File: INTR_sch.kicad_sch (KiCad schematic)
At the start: 10 parts, among them U18 8259A

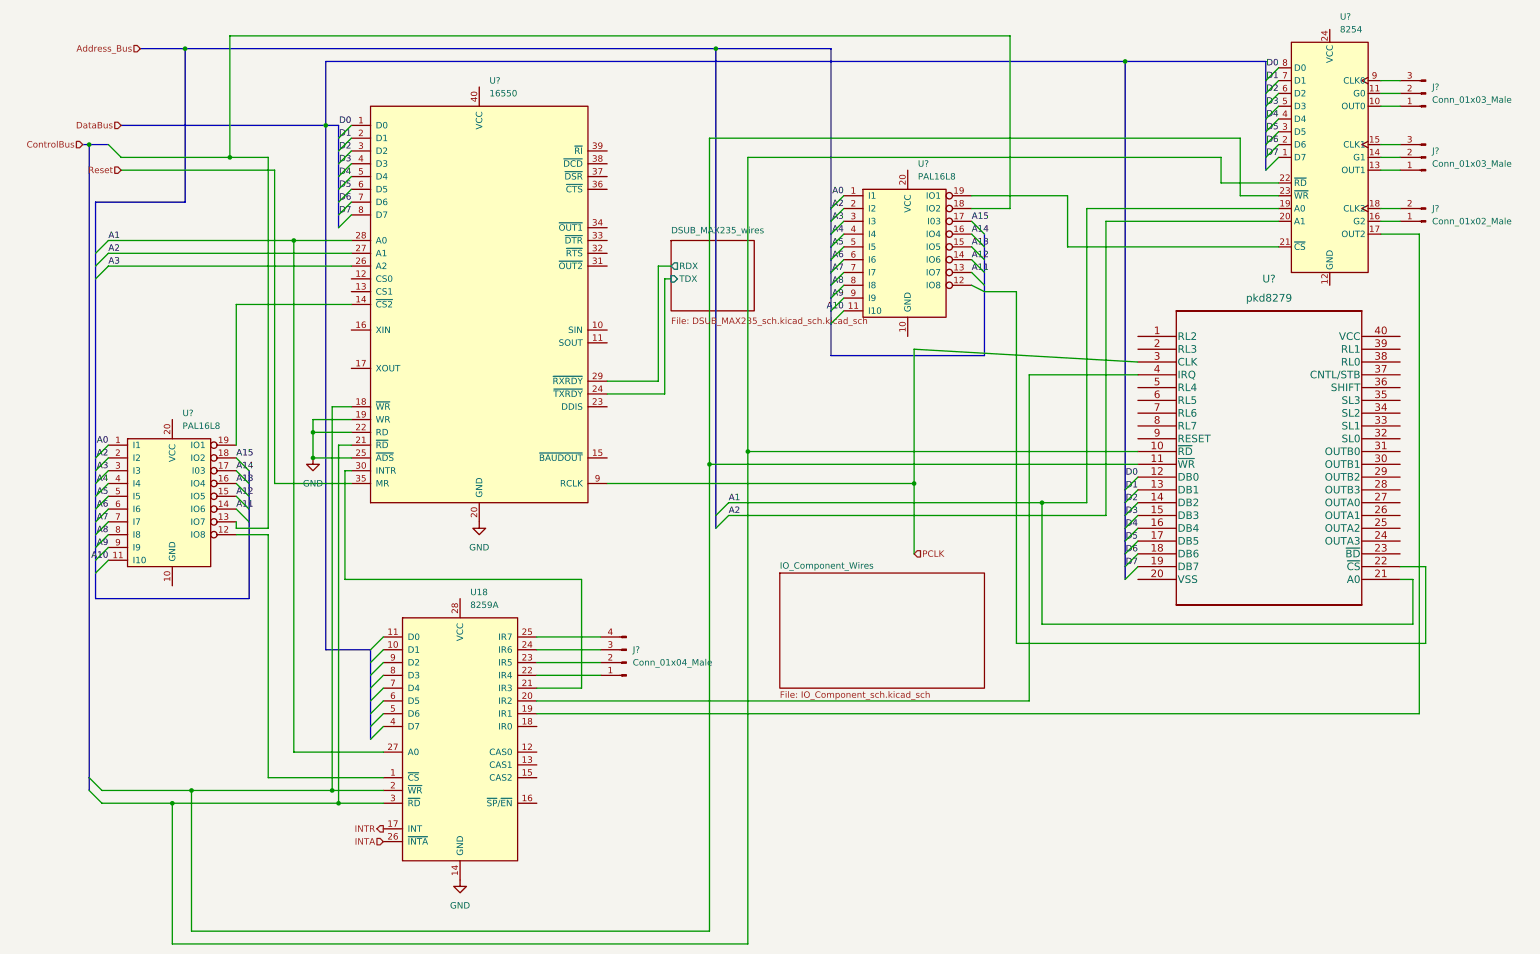
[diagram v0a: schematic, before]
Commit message: Fixed some wires
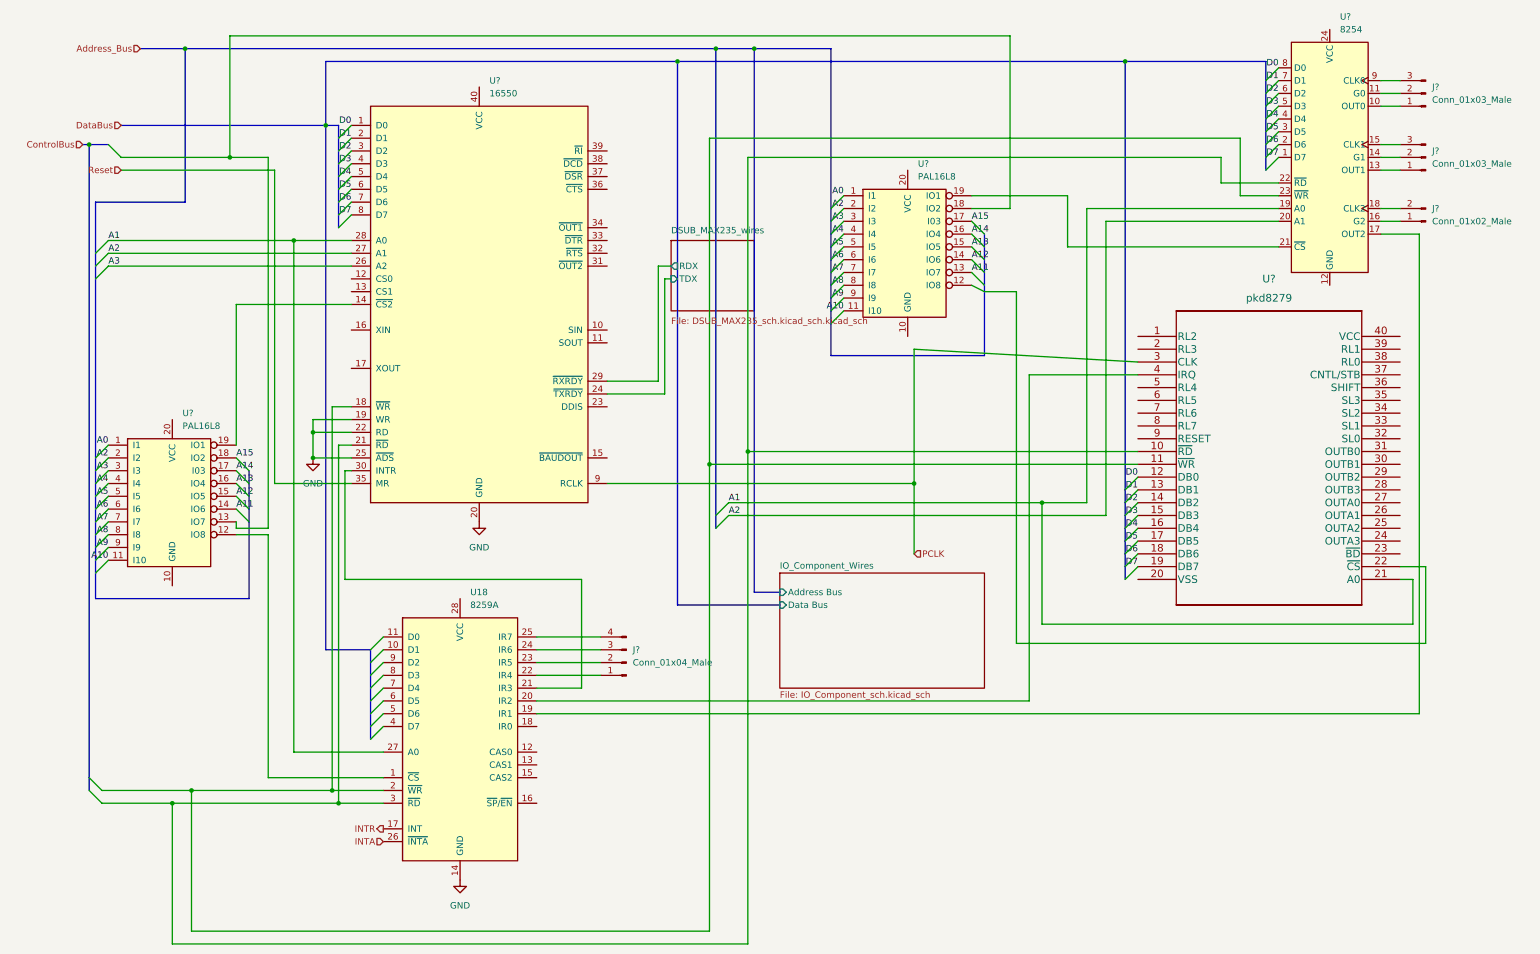
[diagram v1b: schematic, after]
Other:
- sheet IO_Component_Wires ports: added Address Bus, Data Bus; removed none
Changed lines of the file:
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@@
   (junction (at 62.23 93.98) (diameter 0) (color 0 0 0 0)
   )
+  (junction (at 149.86 17.78) (diameter 0) (color 0 0 0 0)
+  )
   (junction (at 66.04 165.1) (diameter 0) (color 0 0 0 0)
   )
+  (junction (at 134.62 20.32) (diameter 0) (color 0 0 0 0)
+  )
   (bus_entry (at 142.24 113.03) (size 2.54 -2.54)
     (stroke (width 0) (type default) (color 0 0 0 0))
@@
     (stroke (width 0) (type default) (color 0 0 0 0))
   )
+  (bus (pts (xy 134.62 128.27) (xy 154.94 128.27))
+    (stroke (width 0) (type default) (color 0 0 0 0))
+  )
   (wire (pts (xy 144.78 107.95) (xy 207.01 107.95))
     (stroke (width 0) (type default) (color 0 0 0 0))
@@
     (stroke (width 0) (type default) (color 0 0 0 0))
   )
+  (bus (pts (xy 134.62 20.32) (xy 134.62 128.27))
+    (stroke (width 0) (type default) (color 0 0 0 0))
+  )
   (bus (pts (xy 73.66 137.16) (xy 64.77 137.16))
     (stroke (width 0) (type default) (color 0 0 0 0))
@@
     (stroke (width 0) (type default) (color 0 0 0 0))
   )
-  (bus (pts (xy 142.24 17.78) (xy 165.1 17.78))
+  (bus (pts (xy 142.24 17.78) (xy 149.86 17.78))
     (stroke (width 0) (type default) (color 0 0 0 0))
   )
@@
     (stroke (width 0) (type default) (color 0 0 0 0))
   )
+  (bus (pts (xy 149.86 125.73) (xy 154.94 125.73))
+    (stroke (width 0) (type default) (color 0 0 0 0))
+  )
   (wire (pts (xy 34.29 167.64) (xy 34.29 195.58))
     (stroke (width 0) (type default) (color 0 0 0 0))
@@
     (stroke (width 0) (type default) (color 0 0 0 0))
   )
+  (bus (pts (xy 149.86 17.78) (xy 165.1 17.78))
+    (stroke (width 0) (type default) (color 0 0 0 0))
+  )
   (wire (pts (xy 45.72 39.37) (xy 53.34 39.37))
     (stroke (width 0) (type default) (color 0 0 0 0))
@@
     (stroke (width 0) (type default) (color 0 0 0 0))
   )
+  (bus (pts (xy 134.62 20.32) (xy 223.52 20.32))
+    (stroke (width 0) (type default) (color 0 0 0 0))
+  )
   (bus (pts (xy 19.05 99.06) (xy 19.05 63.5))
     (stroke (width 0) (type default) (color 0 0 0 0))
@@
     (stroke (width 0) (type default) (color 0 0 0 0))
   )
-  (bus (pts (xy 64.77 20.32) (xy 223.52 20.32))
+  (bus (pts (xy 64.77 20.32) (xy 134.62 20.32))
     (stroke (width 0) (type default) (color 0 0 0 0))
   )
@@
   )
   (bus (pts (xy 49.53 104.14) (xy 49.53 106.68))
+    (stroke (width 0) (type default) (color 0 0 0 0))
+  )
+  (bus (pts (xy 149.86 17.78) (xy 149.86 125.73))
     (stroke (width 0) (type default) (color 0 0 0 0))
   )
@@
       (effects (font (size 1.27 1.27)) (justify left top))
     )
-  )
+    (pin "Address Bus" input (at 154.94 125.73 180)
+      (effects (font (size 1.27 1.27)) (justify left))
+    )
+    (pin "Data Bus" input (at 154.94 128.27 180)
+      (effects (font (size 1.27 1.27)) (justify left))
+    )
+  )

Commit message: Finished wiring and decoding IO devices (except for push button switches)
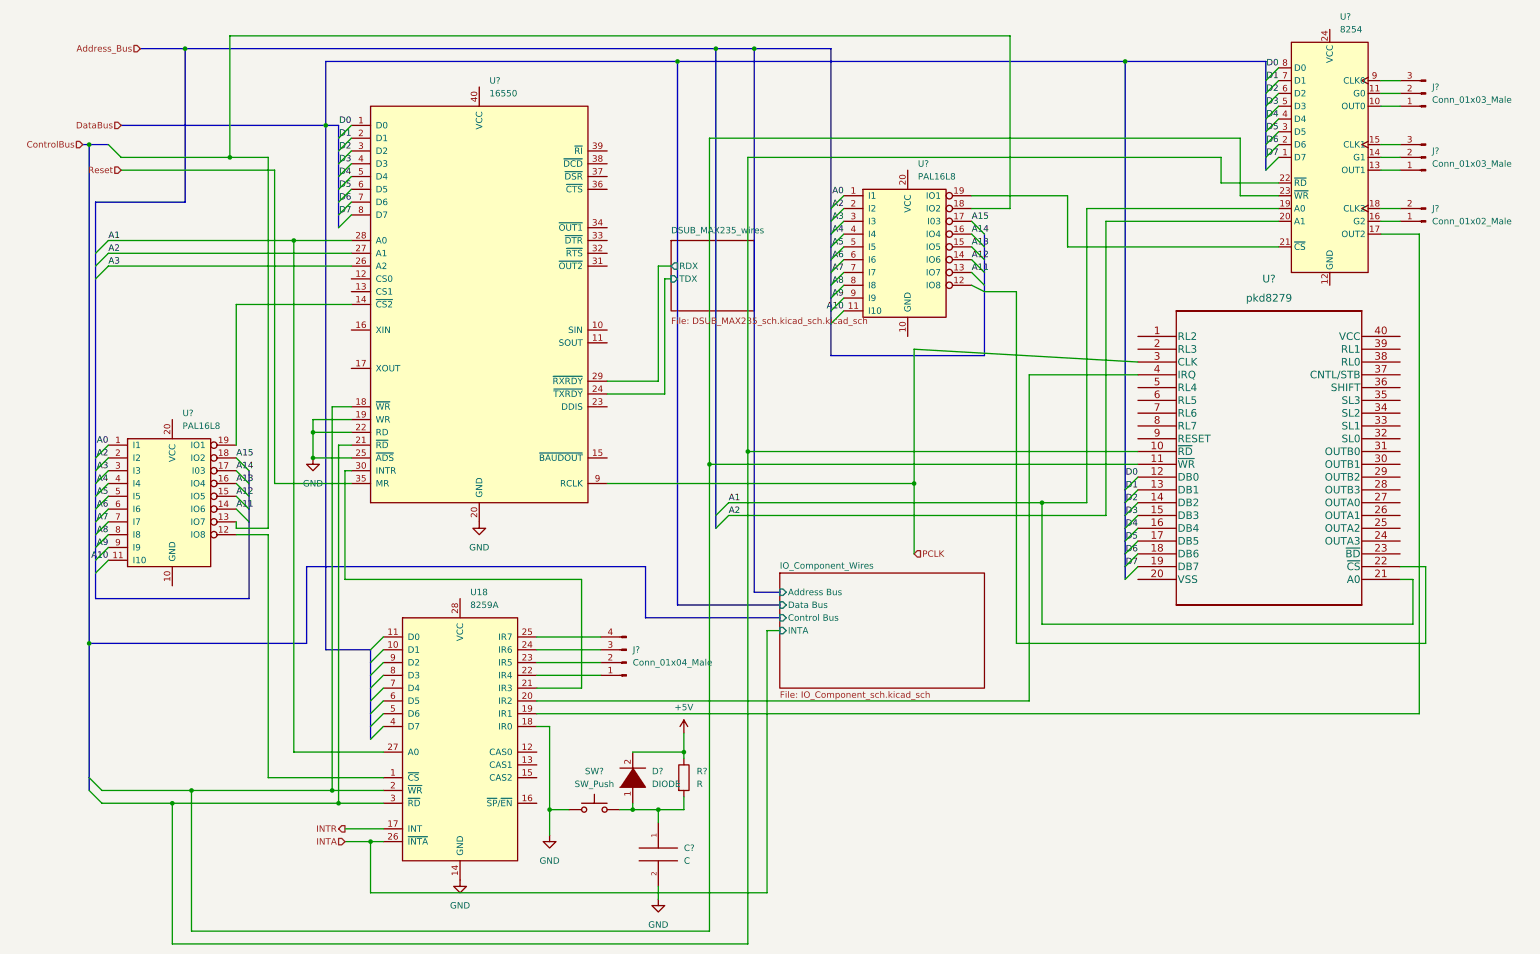
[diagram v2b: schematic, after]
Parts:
- added C?: C, symbol pspice:C
- added D?: DIODE, symbol pspice:DIODE
- added R?: R, symbol Device:R
- added SW?: SW_Push, symbol Switch:SW_Push
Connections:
- net GND: now also U18.18 (IR0), C?.2, SW?.1
- new net: C?.1, D?.1 (K), R?.2, SW?.2
- new net +5V: D?.2 (A), R?.1
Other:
- sheet IO_Component_Wires ports: added Control Bus, INTA; removed none

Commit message: Wired Push Buttons and added footprints
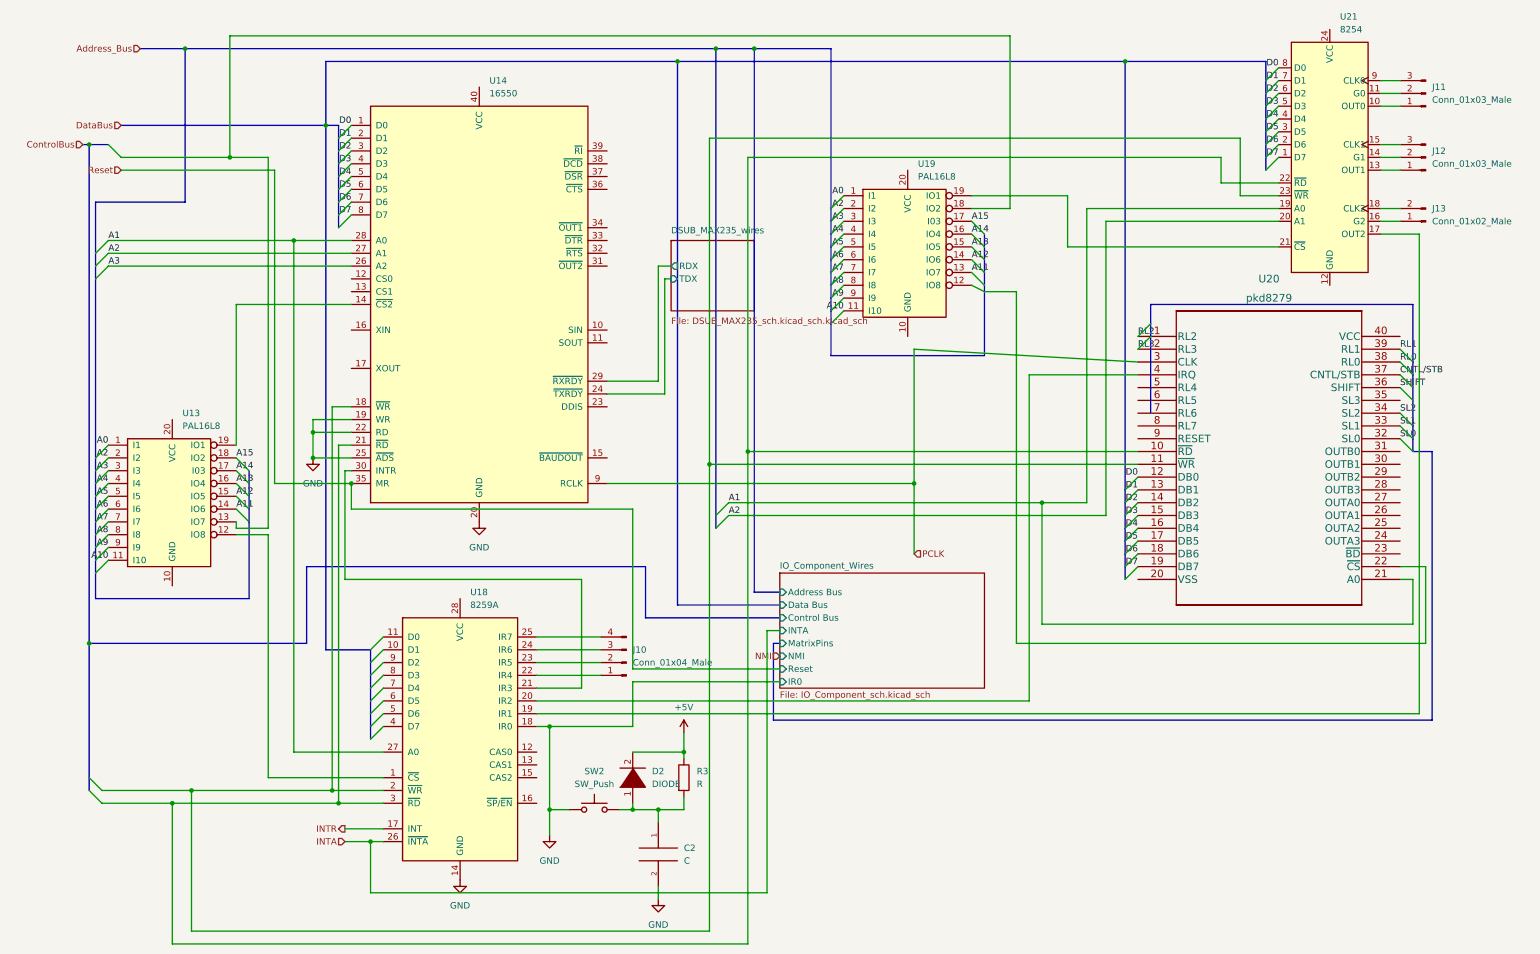
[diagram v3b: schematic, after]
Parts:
- U20: renamed from U?; footprint pkd8279 -> (none)
- gave numbers to parts that had none: 12
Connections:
- net RL2: now reaches U20.1 (RL2)
- net RL3: now reaches U20.2 (RL3)
- net SL0: now reaches U20.32 (SL0)
- net SL1: now reaches U20.33 (SL1)
- net SL2: now reaches U20.34 (SL2)
- net SHIFT: now reaches U20.36 (SHIFT)
- net CNTL/STB: now reaches U20.37 (CNTL/STB)
- net RL0: now reaches U20.38 (RL0)
- net RL1: now reaches U20.39 (RL1)
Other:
- sheet IO_Component_Wires ports: added IR0, MatrixPins, NMI, Reset; removed none

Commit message: Added power and ground to chips
Added power and ground to chips as well as checked and added all labels for pins off of busses
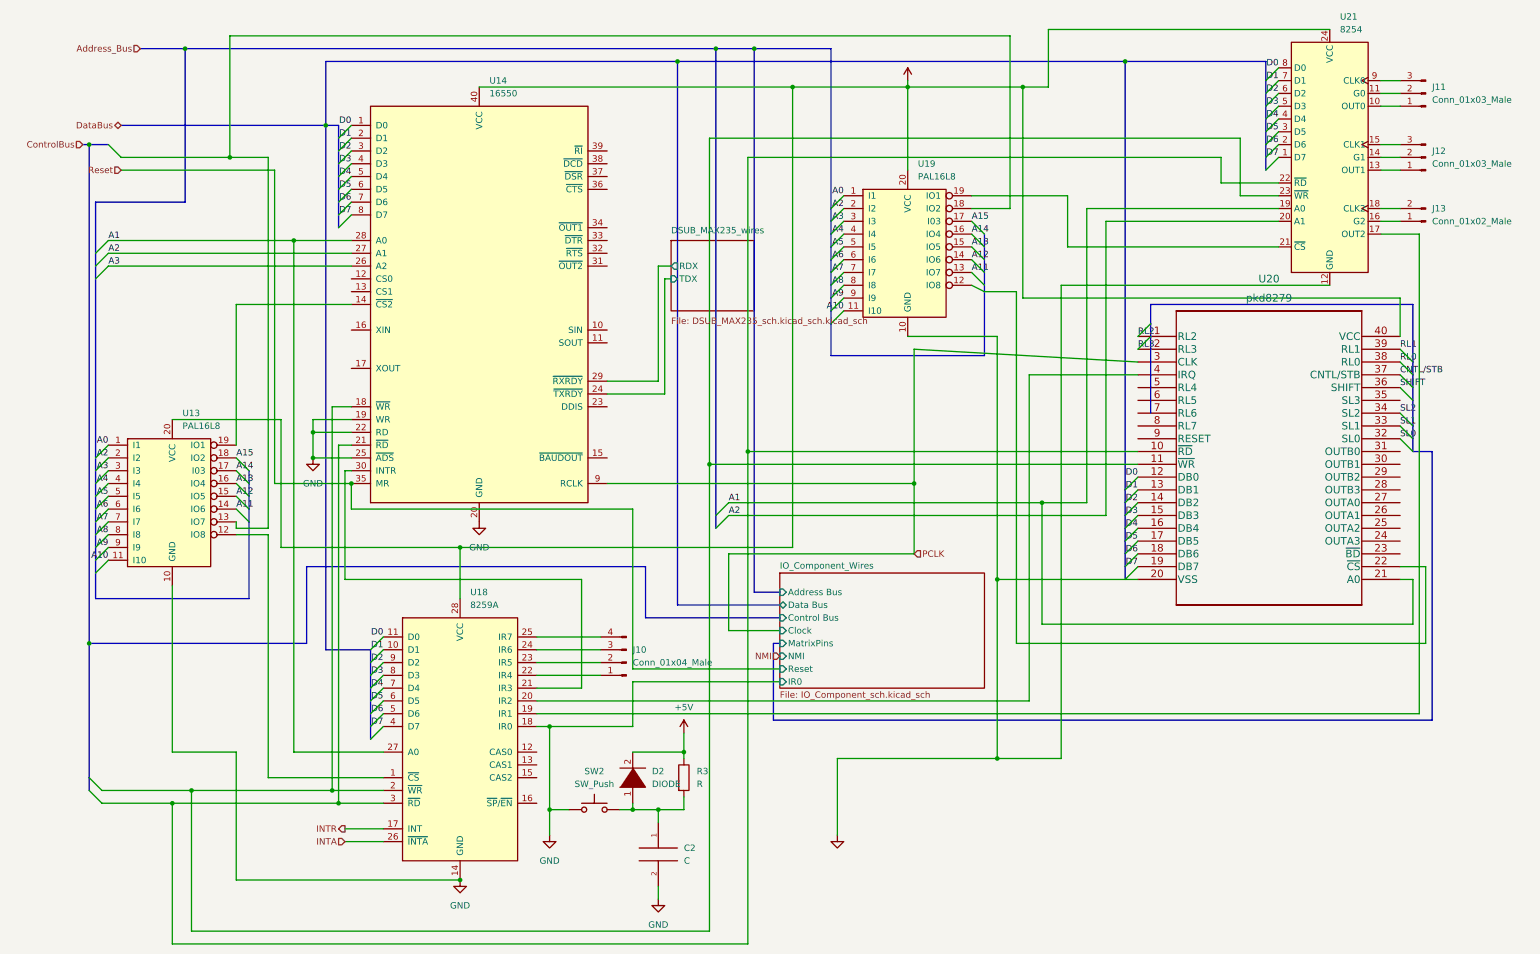
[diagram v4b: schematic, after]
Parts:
- C2: footprint (none) -> Capacitor_SMD:CP_Elec_3x5.3
- D2: footprint (none) -> Diode_SMD:D_0201_0603Metric
- J10, J11, J12, J13: footprint (none) -> Connector_Harwin:Harwin_M20-89008xx_1x08_P2.54mm_Horizontal
- R3: footprint (none) -> Resistor_SMD:R_0201_0603Metric
- SW2: footprint (none) -> Button_Switch_Keyboard:SW_Cherry_MX_1.00u_PCB
- U13, U19: footprint (none) -> Package_DIP:DIP-20_W7.62mm
- U20: footprint (none) -> parts:pkd8279
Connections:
- net +5V: now also U13.20 (VCC), U14.40 (VCC), U18.28 (VCC), U19.20 (VCC), U20.40 (VCC), U21.24 (VCC)
- net D0: now also U18.11 (D0)
- net D1: now also U18.10 (D1)
- net D2: now also U18.9 (D2)
- net D3: now also U18.8 (D3)
- net D4: now also U18.7 (D4)
- net D5: now also U18.6 (D5)
- net D6: now also U18.5 (D6)
- net D7: now also U18.4 (D7)
- net GND: now also U13.10 (GND), U19.10 (GND), U20.20 (VSS), U21.12 (GND)
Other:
- sheet IO_Component_Wires ports: added Clock; removed INTA
